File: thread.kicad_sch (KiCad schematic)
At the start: 21 parts, among them U3001 nRF52840, Y3001 32.768kHz, Y3002 32MHz

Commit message: Finished overall schematic. Fixing errors and warnings from ERC
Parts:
- added C3014: C, symbol Device:C
- added J3001: Conn_Coaxial, symbol Connector:Conn_Coaxial
- added J3002: TC2050, Connector:Tag-Connect_TC2050-IDC-NL_2x05_P1.27mm_Vertical, symbol Connector:TC2050
- added J3003: Conn_01x06_Pin, symbol Connector:Conn_01x06_Pin
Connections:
- net GND: now also C3014.2, J3001.2 (Ext), J3002.3, J3002.5
- net VDD_nRF: now also J3002.1
- net nRF_SWDCLK: now also J3002.4
- net nRF_SWDIO: now also J3002.2
- net at C3009.1, L3004.1: now also C3014.1, J3001.1 (In)
- net nRF_RESET_N: now reaches U3001.AC13 (P0.18/~{RESET})
- net nRF_RESET_N: now also J3002.10
- net IO25: now reaches U3001.AC21 (P0.25)
- net IO25: now also J3003.4 (Pin_4)
- net IO24: now reaches U3001.AD20 (P0.24)
- net IO24: now also J3003.3 (Pin_3)
- net IO26/SDA: now reaches U3001.G1 (P0.26)
- net IO26/SDA: now also J3003.5 (Pin_5)
- net IO27/SCL: now reaches U3001.H2 (P0.27)
- net IO27/SCL: now also J3003.6 (Pin_6)
- net IO6/TX: now reaches U3001.L1 (P0.06)
- net IO6/TX: now also J3003.1 (Pin_1)
- net IO8/RX: now reaches U3001.N1 (P0.08)
- net IO8/RX: now also J3003.2 (Pin_2)
- no-connect marks 6 -> 45
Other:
- note added: "C3014: For potential tuning of pi network"

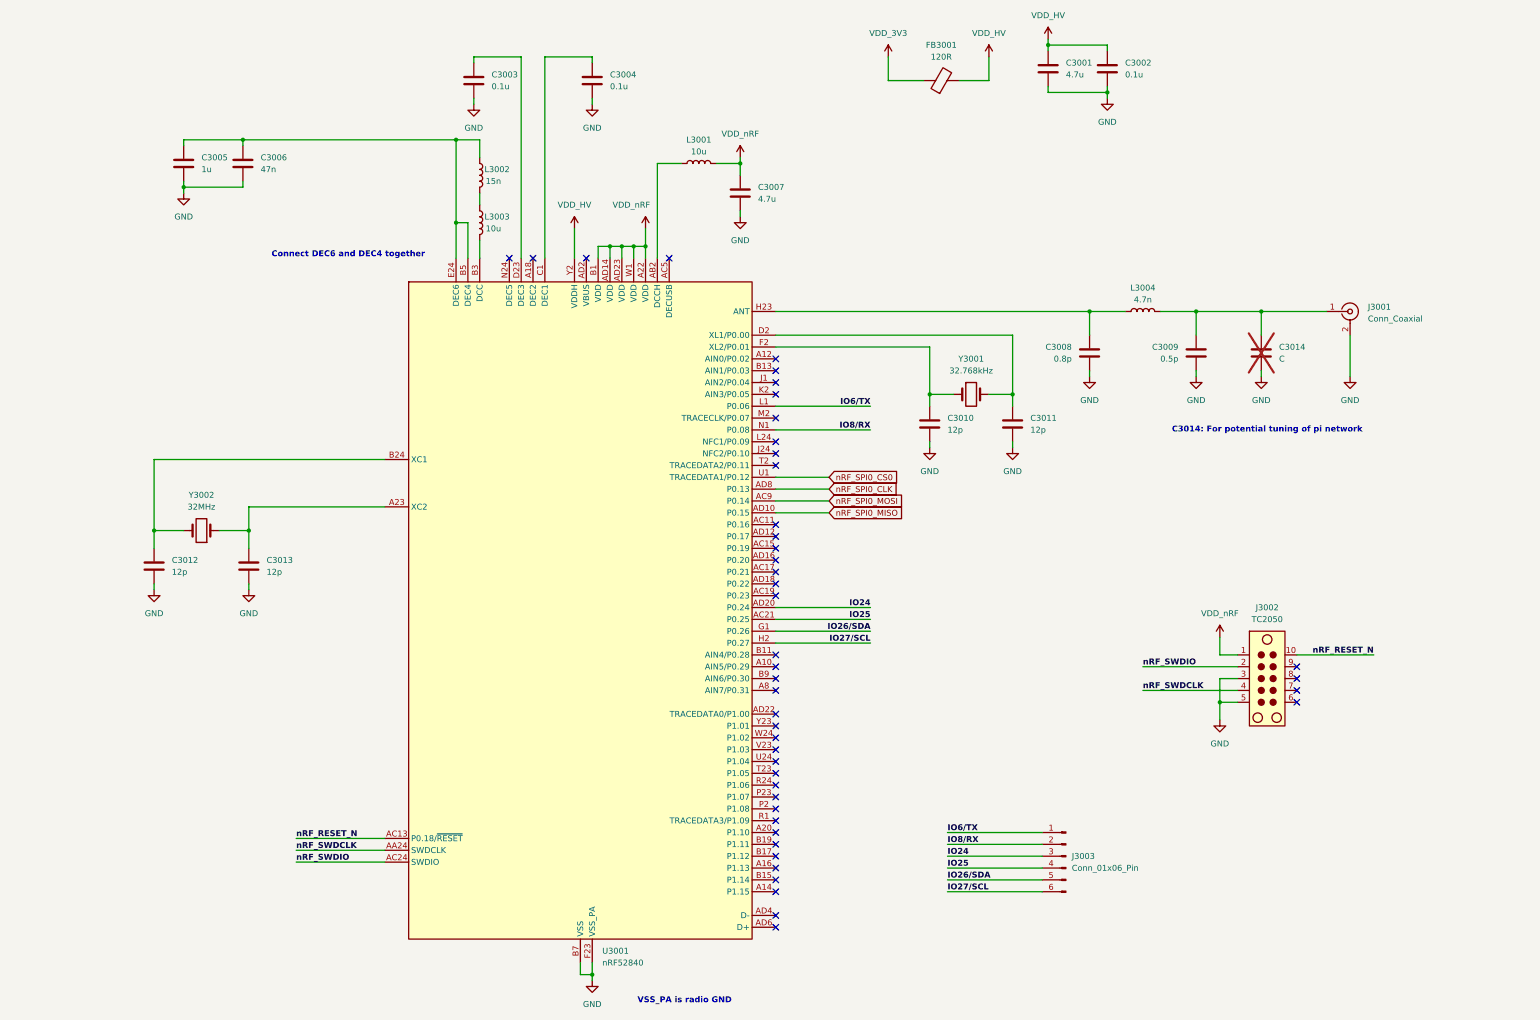
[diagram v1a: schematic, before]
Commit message: Fixed ERC errors and warnings (zero errors and zero warnings)
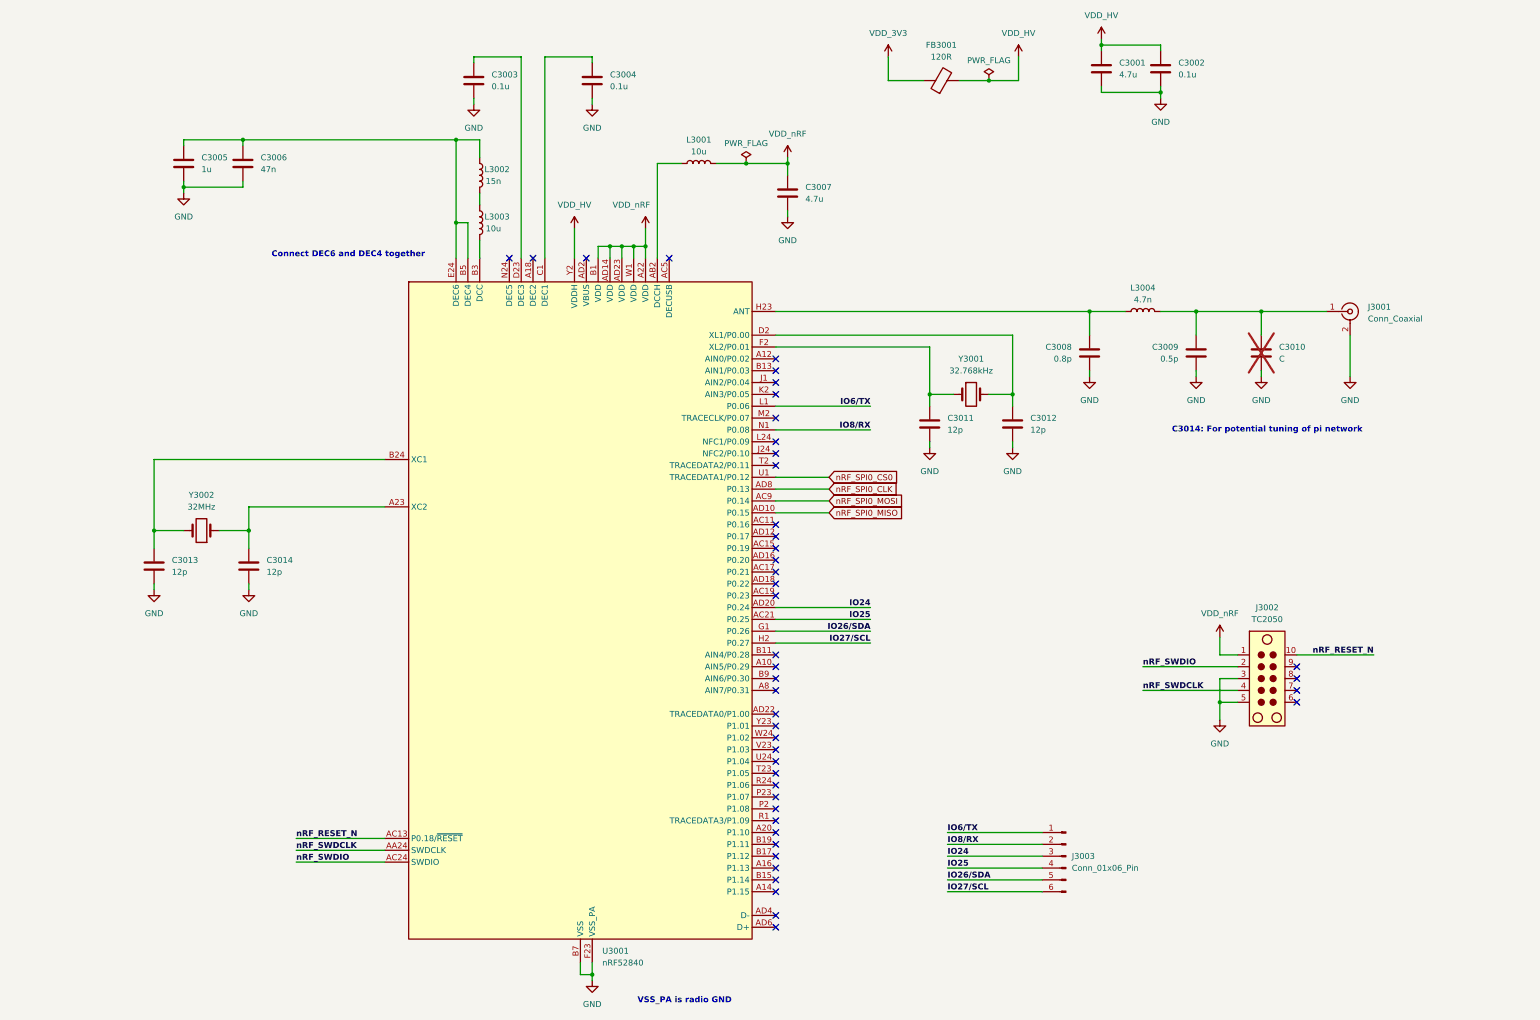
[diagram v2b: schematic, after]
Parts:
- renumbered C3014 to C3010, C3010 to C3011, C3011 to C3012, C3012 to C3013, C3013 to C3014
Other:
- moved on the sheet: C3001, C3002, C3007

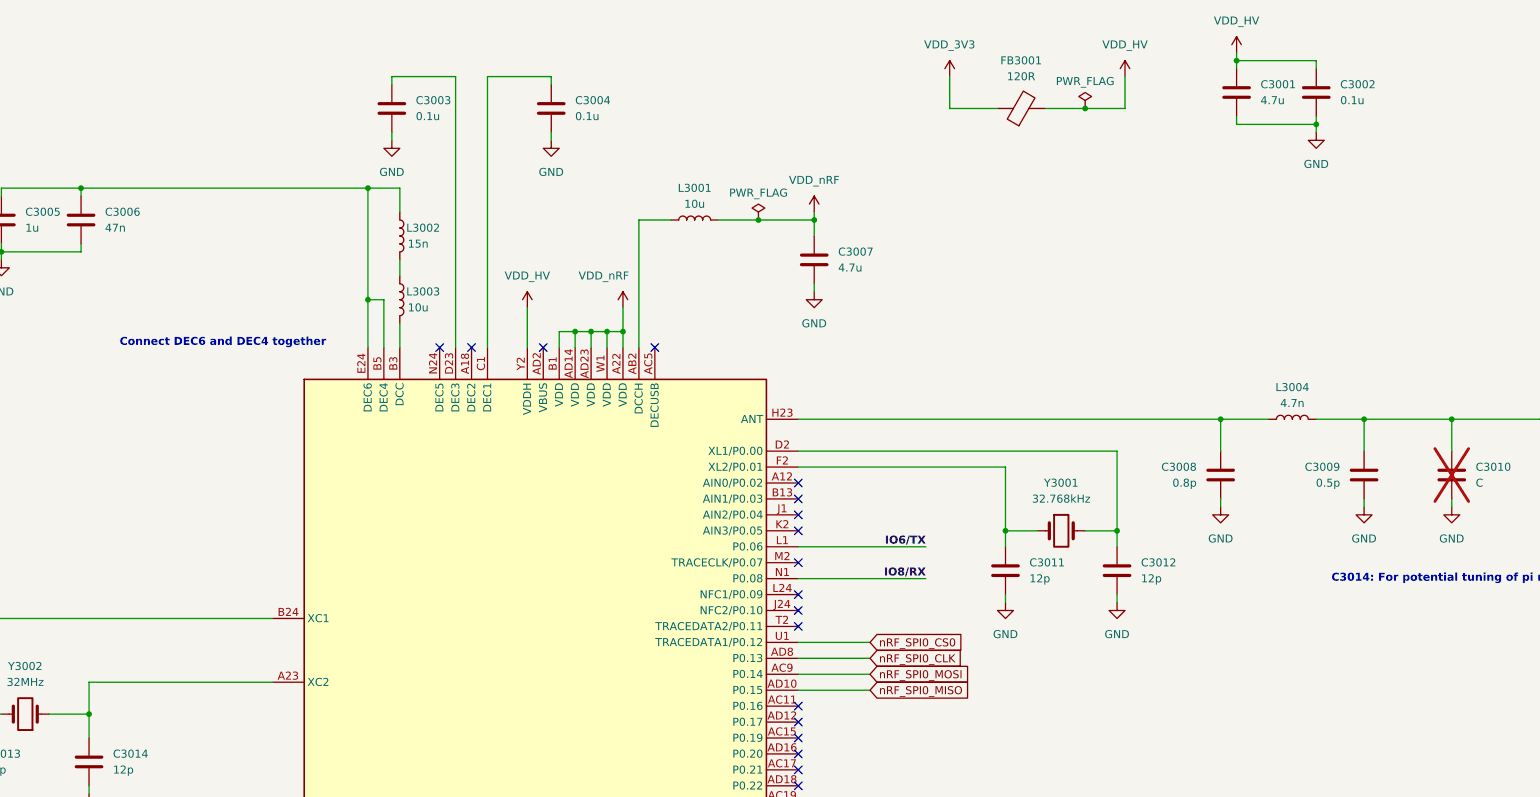
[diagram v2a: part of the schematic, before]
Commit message: Labeled all nets and added some footprints
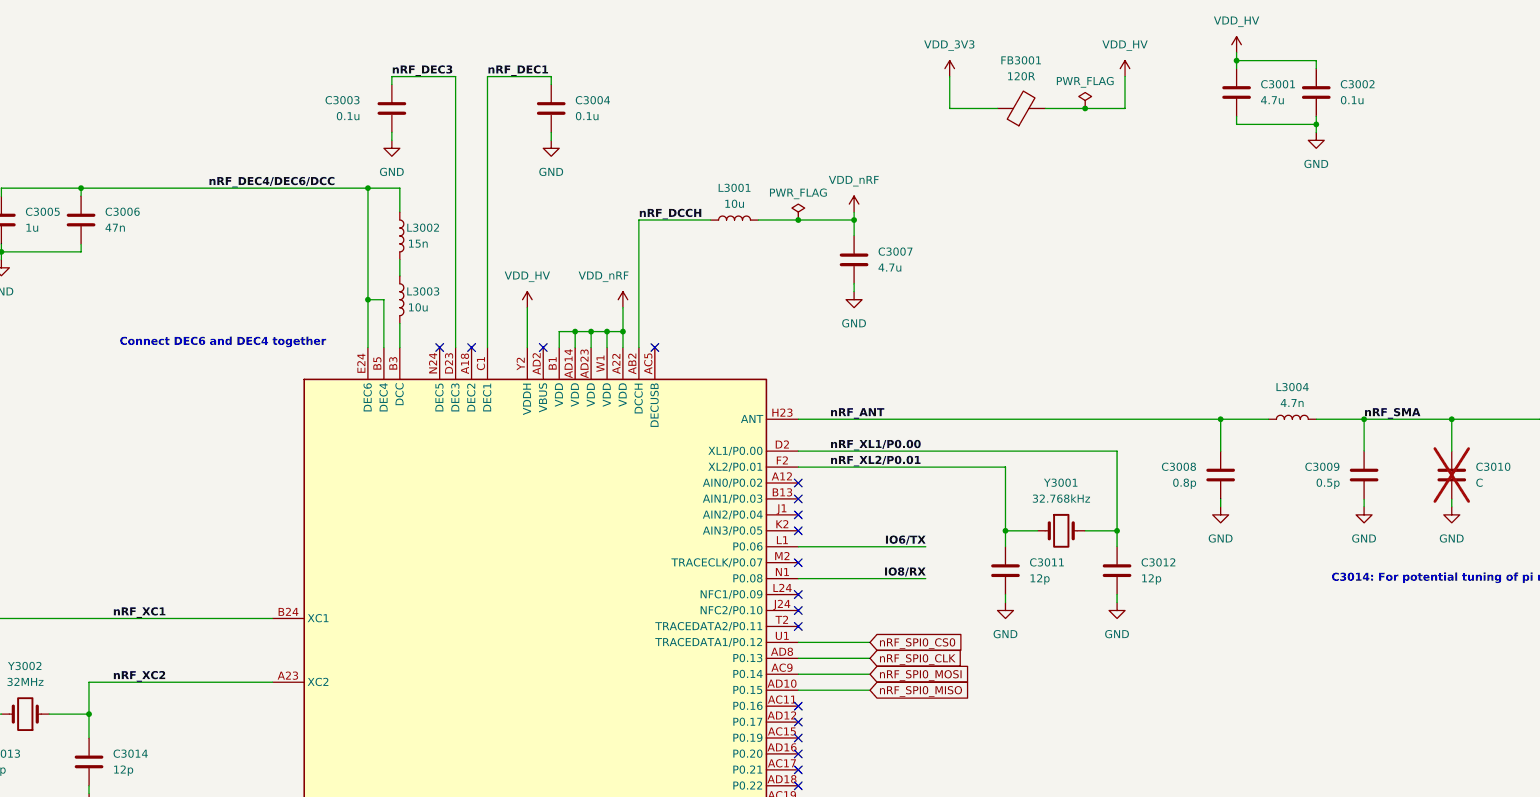
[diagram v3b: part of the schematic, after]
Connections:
- net nRF_SMA: now reaches C3009.1, C3010.1, J3001.1 (In), L3004.1
- net nRF_ANT: now reaches C3008.1, L3004.2, U3001.H23 (ANT)
- net nRF_DEC4/DEC6/DCC: now reaches C3005.1, C3006.1, L3002.1, U3001.B5 (DEC4), U3001.E24 (DEC6)
- net nRF_XL2/P0.01: now reaches C3011.1, U3001.F2 (XL2/P0.01), Y3001.1
- net nRF_DEC3: now reaches C3003.1, U3001.D23 (DEC3)
- net nRF_XC2: now reaches C3014.1, U3001.A23 (XC2), Y3002.1
- net nRF_DCCH: now reaches L3001.1, U3001.AB2 (DCCH)
- net nRF_XC1: now reaches C3013.1, U3001.B24 (XC1), Y3002.2
- net nRF_DEC1: now reaches C3004.1, U3001.C1 (DEC1)
- net nRF_XL1/P0.00: now reaches C3012.1, U3001.D2 (XL1/P0.00), Y3001.2
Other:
- moved on the sheet: C3007, L3001
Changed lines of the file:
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@@
 	)
 	(junction
-		(at 195.58 74.93)
+		(at 201.93 74.93)
 		(diameter 0)
 		(color 0 0 0 0)
@@
 	)
 	(junction
-		(at 186.69 74.93)
+		(at 193.04 74.93)
 		(diameter 0)
 		(color 0 0 0 0)
@@
 	(wire
 		(pts
+			(xy 128.27 52.07) (xy 138.43 52.07)
+		)
+		(stroke
+			(width 0)
+			(type default)
+		)
+	)
+	(wire
+		(pts
 			(xy 160.02 92.71) (xy 160.02 95.25)
 		)
@@
 	(wire
 		(pts
-			(xy 138.43 52.07) (xy 128.27 52.07)
-		)
-		(stroke
-			(width 0)
-			(type default)
-		)
-	)
-	(wire
-		(pts
 			(xy 297.18 106.68) (xy 283.21 106.68)
 		)
@@
 	(wire
 		(pts
-			(xy 167.64 95.25) (xy 167.64 74.93)
+			(xy 167.64 74.93) (xy 167.64 95.25)
 		)
 		(stroke
@@
 	(wire
 		(pts
-			(xy 195.58 74.93) (xy 195.58 77.47)
+			(xy 201.93 74.93) (xy 201.93 77.47)
 		)
 		(stroke
@@
 	(wire
 		(pts
-			(xy 195.58 73.66) (xy 195.58 74.93)
+			(xy 201.93 73.66) (xy 201.93 74.93)
 		)
 		(stroke
@@
 	(wire
 		(pts
-			(xy 167.64 74.93) (xy 172.72 74.93)
+			(xy 167.64 74.93) (xy 179.07 74.93)
 		)
 		(stroke
@@
 	(wire
 		(pts
-			(xy 195.58 85.09) (xy 195.58 86.36)
+			(xy 201.93 85.09) (xy 201.93 86.36)
 		)
 		(stroke
@@
 	(wire
 		(pts
-			(xy 186.69 74.93) (xy 195.58 74.93)
+			(xy 193.04 74.93) (xy 201.93 74.93)
 		)
 		(stroke
@@
 	(wire
 		(pts
-			(xy 180.34 74.93) (xy 186.69 74.93)
+			(xy 186.69 74.93) (xy 193.04 74.93)
 		)
 		(stroke
@@
 		)
 	)
+	(label "nRF_XC2"
+		(at 83.82 148.59 0)
+		(effects
+			(font
+				(size 1.27 1.27)
+				(thickness 0.254)
+				(bold yes)
+			)
+			(justify left bottom)
+		)
+	)
+	(label "nRF_XL1{slash}P0.00"
+		(at 198.12 111.76 0)
+		(effects
+			(font
+				(size 1.27 1.27)
+				(thickness 0.254)
+				(bold yes)
+			)
+			(justify left bottom)
+		)
+	)
 	(label "nRF_SWDIO"
 		(at 271.78 182.88 0)
@@
 		)
 	)
+	(label "nRF_DCCH"
+		(at 167.64 74.93 0)
+		(effects
+			(font
+				(size 1.27 1.27)
+				(thickness 0.254)
+				(bold yes)
+			)
+			(justify left bottom)
+		)
+	)
 	(label "IO8{slash}RX"
 		(at 213.36 132.08 180)
@@
 		)
 	)
+	(label "nRF_XC1"
+		(at 83.82 138.43 0)
+		(effects
+			(font
+				(size 1.27 1.27)
+				(thickness 0.254)
+				(bold yes)
+			)
+			(justify left bottom)
+		)
+	)
+	(label "nRF_DEC1"
+		(at 143.51 52.07 0)
+		(effects
+			(font
+				(size 1.27 1.27)
+				(thickness 0.254)
+				(bold yes)
+			)
+			(justify left bottom)
+		)
+	)
+	(label "nRF_ANT"
+		(at 198.12 106.68 0)
+		(effects
+			(font
+				(size 1.27 1.27)
+				(thickness 0.254)
+				(bold yes)
+			)
+			(justify left bottom)
+		)
+	)
+	(label "nRF_DEC3"
+		(at 128.27 52.07 0)
+		(effects
+			(font
+				(size 1.27 1.27)
+				(thickness 0.254)
+				(bold yes)
+			)
+			(justify left bottom)
+		)
+	)
+	(label "nRF_XL2{slash}P0.01"
+		(at 198.12 114.3 0)
+		(effects
+			(font
+				(size 1.27 1.27)
+				(thickness 0.254)
+				(bold yes)
+			)
+			(justify left bottom)
+		)
+	)
 	(label "IO27{slash}SCL"
 		(at 213.36 177.8 180)
@@
 		)
 	)
+	(label "nRF_DEC4{slash}DEC6{slash}DCC"
+		(at 99.06 69.85 0)
+		(effects
+			(font
+				(size 1.27 1.27)
+				(thickness 0.254)
+				(bold yes)
+			)
+			(justify left bottom)
+		)
+	)
 	(label "IO26{slash}SDA"
 		(at 213.36 175.26 180)
@@
 		)
 	)
+	(label "nRF_SMA"
+		(at 283.21 106.68 0)
+		(effects
+			(font
+				(size 1.27 1.27)
+				(thickness 0.254)
+				(bold yes)
+			)
+			(justify left bottom)
+		)
+	)
 	(global_label "nRF_SPI0_CLK"
 		(shape input)
@@
 	(symbol
 		(lib_id "power:VDD")
-		(at 195.58 73.66 0)
+		(at 201.93 73.66 0)
 		(unit 1)
 		(exclude_from_sim no)
@@
 		(fields_autoplaced yes)
 		(property "Reference" "#PWR03007"
-			(at 195.58 77.47 0)
+			(at 201.93 77.47 0)
 			(effects
 				(font
@@
 		)
 		(property "Value" "VDD_nRF"
-			(at 195.58 68.58 0)
+			(at 201.93 68.58 0)
 			(effects
 				(font
@@
 		)
 		(property "Footprint" ""
-			(at 195.58 73.66 0)
+			(at 201.93 73.66 0)
 			(effects
 				(font
@@
 		)
 		(property "Datasheet" ""
-			(at 195.58 73.66 0)
+			(at 201.93 73.66 0)
 			(effects
 				(font
@@
 		)
 		(property "Description" "Power symbol creates a global label with name \"VDD\""
-			(at 195.58 73.66 0)
+			(at 201.93 73.66 0)
 			(effects
 				(font
@@
 	(symbol
 		(lib_id "power:PWR_FLAG")
-		(at 186.69 74.93 0)
+		(at 193.04 74.93 0)
 		(unit 1)
 		(exclude_from_sim no)
@@
 		(dnp no)
 		(property "Reference" "#FLG04041"
-			(at 186.69 73.025 0)
+			(at 193.04 73.025 0)
 			(effects
 				(font
@@
 		)
 		(property "Value" "PWR_FLAG"
-			(at 186.69 70.612 0)
+			(at 193.04 70.612 0)
 			(effects
 				(font
@@
 		)
 		(property "Footprint" ""
-			(at 186.69 74.93 0)
+			(at 193.04 74.93 0)
 			(effects
 				(font
@@
 		)
 		(property "Datasheet" "~"
-			(at 186.69 74.93 0)
+			(at 193.04 74.93 0)
 			(effects
 				(font
@@
 		)
 		(property "Description" "Special symbol for telling ERC where power comes from"
-			(at 186.69 74.93 0)
+			(at 193.04 74.93 0)
 			(effects
 				(font
@@
 		(on_board yes)
 		(dnp no)
-		(fields_autoplaced yes)
 		(property "Reference" "C3003"
-			(at 132.08 55.8799 0)
+			(at 117.602 55.88 0)
 			(effects
 				(font
@@
 		)
 		(property "Value" "0.1u"
-			(at 132.08 58.4199 0)
+			(at 119.38 58.42 0)
 			(effects
 				(font
@@
 	(symbol
 		(lib_id "power:GND")
-		(at 195.58 86.36 0)
+		(at 201.93 86.36 0)
 		(unit 1)
 		(exclude_from_sim no)
@@
 		(fields_autoplaced yes)
 		(property "Reference" "#PWR03009"
-			(at 195.58 92.71 0)
+			(at 201.93 92.71 0)
 			(effects
 				(font
@@
 		)
 		(property "Value" "GND"
-			(at 195.58 91.44 0)
+			(at 201.93 91.44 0)
 			(effects
 				(font
@@
 		)
 		(property "Footprint" ""
-			(at 195.58 86.36 0)
+			(at 201.93 86.36 0)
 			(effects
 				(font
@@
 		)
 		(property "Datasheet" ""
-			(at 195.58 86.36 0)
+			(at 201.93 86.36 0)
 			(effects
 				(font
@@
 		)
 		(property "Description" "Power symbol creates a global label with name \"GND\" , ground"
-			(at 195.58 86.36 0)
+			(at 201.93 86.36 0)
 			(effects
 				(font
@@
 	(symbol
 		(lib_id "Device:L")
-		(at 176.53 74.93 90)
+		(at 182.88 74.93 90)
 		(unit 1)
 		(exclude_from_sim no)
@@
 		(fields_autoplaced yes)
 		(property "Reference" "L3001"
-			(at 176.53 69.85 90)
+			(at 182.88 69.85 90)
 			(effects
 				(font
@@
 		)
 		(property "Value" "10u"
-			(at 176.53 72.39 90)
+			(at 182.88 72.39 90)
 			(effects
 				(font
@@
 		)
 		(property "Footprint" ""
-			(at 176.53 74.93 0)
+			(at 182.88 74.93 0)
 			(effects
 				(font
@@
 		)
 		(property "Datasheet" "~"
-			(at 176.53 74.93 0)
+			(at 182.88 74.93 0)
 			(effects
 				(font
@@
 		)
 		(property "Description" "Inductor"
-			(at 176.53 74.93 0)
+			(at 182.88 74.93 0)
 			(effects
 				(font
@@
 	(symbol
 		(lib_id "Device:C")
-		(at 195.58 81.28 0)
+		(at 201.93 81.28 0)
 		(unit 1)
 		(exclude_from_sim no)
@@
 		(fields_autoplaced yes)
 		(property "Reference" "C3007"
-			(at 199.39 80.0099 0)
+			(at 205.74 80.0099 0)
 			(effects
 				(font
@@
 		)
 		(property "Value" "4.7u"
-			(at 199.39 82.5499 0)
+			(at 205.74 82.5499 0)
 			(effects
 				(font
@@
 		)
 		(property "Footprint" ""
-			(at 196.5452 85.09 0)
+			(at 202.8952 85.09 0)
 			(effects
 				(font
@@
 		)
 		(property "Datasheet" "~"
-			(at 195.58 81.28 0)
+			(at 201.93 81.28 0)
 			(effects
 				(font
@@
 		)
 		(property "Description" "Unpolarized capacitor"
-			(at 195.58 81.28 0)
+			(at 201.93 81.28 0)
 			(effects
 				(font
